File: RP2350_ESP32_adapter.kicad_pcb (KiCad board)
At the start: 2 copper layers, 28 x 61.3 mm, 10 parts, among them U1 RaspberryPi_Pico, U2 T-Display-S3, U3 EMC2302-1, U4 TXU0102-DCU, U5 PCA9536D

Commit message: Finish routing
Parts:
- C1, C2, C3: footprint Capacitor_SMD:C_0805_2012Metric -> Capacitor_SMD:C_0603_1608Metric
- moved R2 1.55 mm to (158.6, 136.1), turned to 90 degrees
- moved C2 0.60 mm to (156.2, 116.2)
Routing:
- net /RESET: track 0.00 -> 54.8 mm
- net +3V3: track 0.04 -> 27.8 mm, vias 0 -> 2
- net /W5500_MISO: track 0.00 -> 25.5 mm
- net Net-(U2-GPIO16): track 0.00 -> 18.7 mm, vias 0 -> 1
- net /RP_TACHO1: track 0.00 -> 8.73 mm, vias 0 -> 1
- net /LDO_EN: track 41.2 -> 47.1 mm, vias 0 -> 2
- net /VR_RDY: track 41.5 -> 45.3 mm
- net /RX: track 26.2 -> 29.1 mm
- net /SDA: track 35.4 -> 37.7 mm, vias 1 -> 2
- net GND: track 0.00 -> 1.65 mm, vias 1 -> 4
- net /SCL: track 37.8 -> 39.4 mm, vias 1 -> 2
- net /W5500_INT_N: track 17.4 -> 16.1 mm
- net Net-(U3-PWM2): track 3.28 -> 4.52 mm
- net /PWR_EN: track 53.6 -> 52.5 mm
- net /RP_TACHO2: track 13.5 -> 12.7 mm, vias 0 -> 1

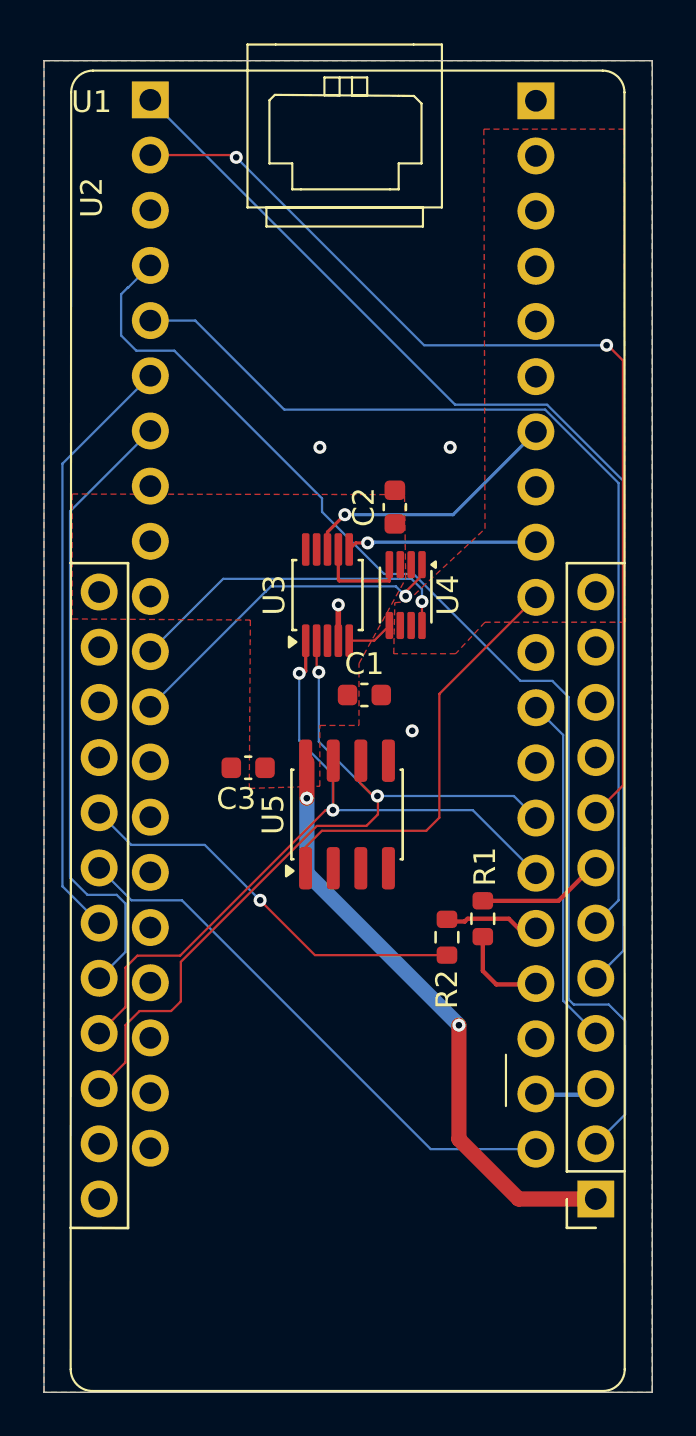
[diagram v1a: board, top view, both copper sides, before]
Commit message: Change ESP32Module to pin socket in PCB
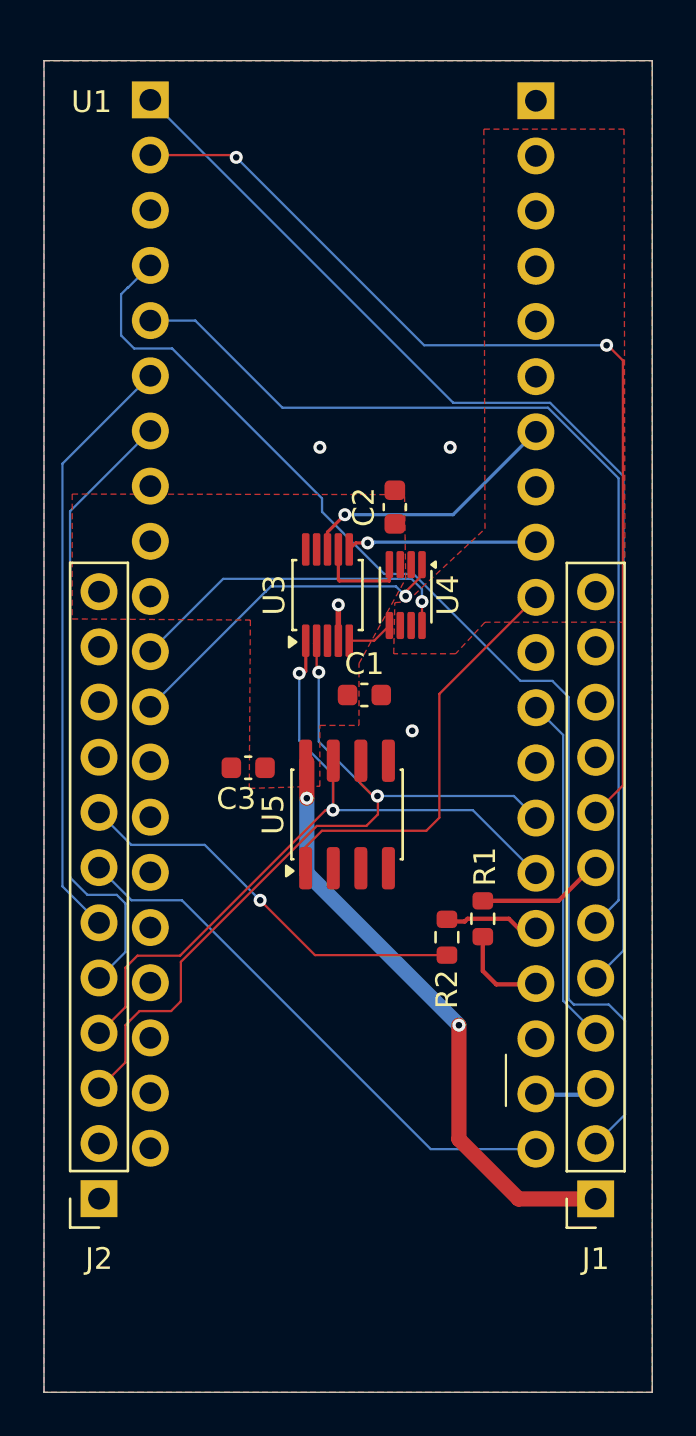
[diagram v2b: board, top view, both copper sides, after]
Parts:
- removed U2: T-Display-S3, ESP32:t-display-s3
- added J1: Conn_01x12_Socket, Connector_PinSocket_2.54mm:PinSocket_1x12_P2.54mm_Vertical, F.Cu at (165.4, 148.1)
- added J2: Conn_01x12_Socket, Connector_PinSocket_2.54mm:PinSocket_1x12_P2.54mm_Vertical, F.Cu at (142.5, 148.1)

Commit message: Modifi solder mask expansion
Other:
- rule pad_to_mask_clearance: 0 -> 0.05
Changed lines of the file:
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@@
 			(dielectric_constraints no)
 		)
-		(pad_to_mask_clearance 0)
+		(pad_to_mask_clearance 0.05)
 		(allow_soldermask_bridges_in_footprints no)
 		(tenting
@@
 		(capping no)
 		(filling no)
+		(zone_defaults)
 		(pcbplotparams
 			(layerselection 0x00000000_00000000_55555555_5755f5ff)
@@
 			(outputformat 1)
 			(mirror no)
-			(drillshape 1)
+			(drillshape 0)
 			(scaleselection 1)
-			(outputdirectory "")
+			(outputdirectory "../gerbers/RP2350_ESP32_adapter/")
 		)
 	)
@@
 			)
 		)
-		(attr through_hole)
+		(attr through_hole dnp)
 		(duplicate_pad_numbers_are_jumpers no)
 		(fp_line

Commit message: Add board name to top
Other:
- board text added: "RP2350 to ESP32 Adapter V1.0.0"
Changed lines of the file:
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@@
 		(layer "Edge.Cuts")
+	)
+	(gr_text "RP2350 to ESP32 Adapter\nV1.0.0"
+		(at 141.025 155.5 0)
+		(layer "F.SilkS")
+		(effects
+			(font
+				(size 1 1)
+				(thickness 0.1)
+			)
+			(justify left bottom)
+		)
 	)
 	(segment
